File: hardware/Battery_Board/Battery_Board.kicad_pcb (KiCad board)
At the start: 2 copper layers, 83 x 83 mm, 28 parts, among them J1 Source, J3 Battery, P1 USB_C_Plug_USB2.0, Q1 DMG3415U-7, SW3 ON, U4 TP4056

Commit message: feat(Hw):PCB_PwnSat_And_Battery_Updated
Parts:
- moved D4 67.6 mm to (67.0, 146.4), turned to 90 degrees
- moved D3 66.3 mm to (69.9, 146.4), turned to 90 degrees
- moved R31 60.1 mm to (72.1, 145.6), turned to 180 degrees
- moved R33 9.93 mm to (117.6, 108.8), turned to 90 degrees
- moved Q1 7.08 mm to (114.3, 114.7), turned to -90 degrees
- moved D2 2.58 mm to (113.3, 111.0), turned to 0 degrees
- moved C48 2.27 mm to (105.8, 109.7)
- moved C49 1.57 mm to (72.1, 154.9), turned to 180 degrees
- moved R32 1.51 mm to (72.7, 153.7)
- moved R34 1.49 mm to (72.7, 152.8), turned to 180 degrees
- moved R26 0.91 mm to (83.2, 113.0)
- moved F1 0.90 mm to (84.6, 113.0)
- moved R27 0.85 mm to (79.2, 112.2), turned to 0 degrees
- turned R29 to -90 degrees
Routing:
- net +BATT: track 0.00 -> 134.2 mm, vias 0 -> 54
- net /Batt_Connector/USB_DET: track 0.00 -> 90.3 mm
- net VBUS: track 0.00 -> 88.7 mm, vias 0 -> 12
- net /Batt_Connector/Battery: track 0.00 -> 71.6 mm, vias 0 -> 2
- net /Batt_Connector/Enable: track 0.00 -> 65.0 mm
- net VCC: track 0.00 -> 59.2 mm, vias 0 -> 15
- net +3.3V: track 0.00 -> 51.7 mm
- net Net-(D4-K): track 0.00 -> 19.5 mm, vias 0 -> 2
- net Net-(D3-K): track 0.00 -> 16.0 mm, vias 0 -> 2
- net Net-(F1-Pad1): track 0.00 -> 10.3 mm
- net Net-(D2-K): track 0.00 -> 9.72 mm
- net /Batt_Connector/2_DN: track 99.2 -> 105.7 mm
- net Net-(U4-PROG): track 0.00 -> 6.16 mm
- net /Batt_Connector/2_DP: track 99.8 -> 106.0 mm
- net Net-(D3-A): track 0.00 -> 4.28 mm
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- added copper zone on F.Cu, net +3.3V
- added copper zone on B.Cu, net +BATT
- added copper zone on F.Cu, net +BATT
- added copper zone on B.Cu, net GND
- added copper zone on F.Cu, net GND
- added copper zone on B.Cu, net VBUS
- added copper zone on F.Cu, net VBUS
- added copper zone on B.Cu, net VCC
- added copper zone on F.Cu, net VCC

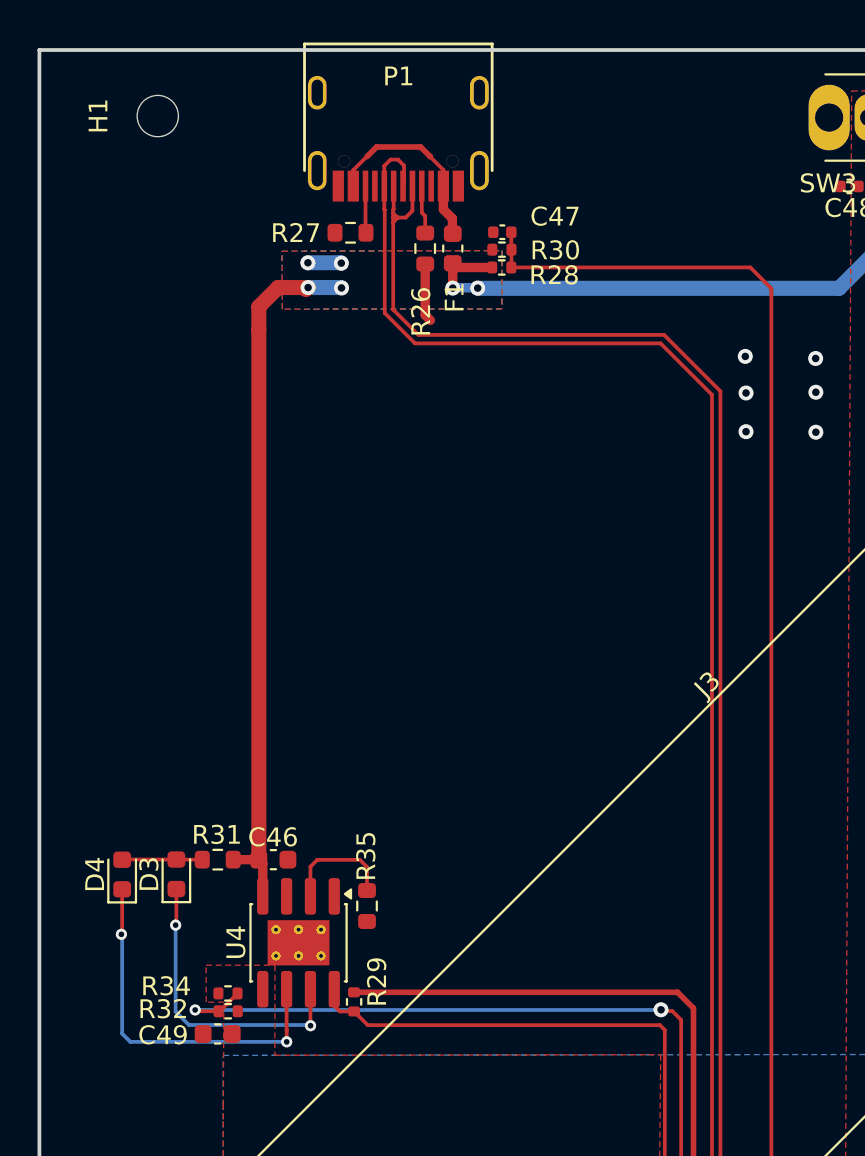
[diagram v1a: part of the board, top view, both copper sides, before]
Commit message: feat(Hw):Boards_Updated
Pending_Sensors_Board
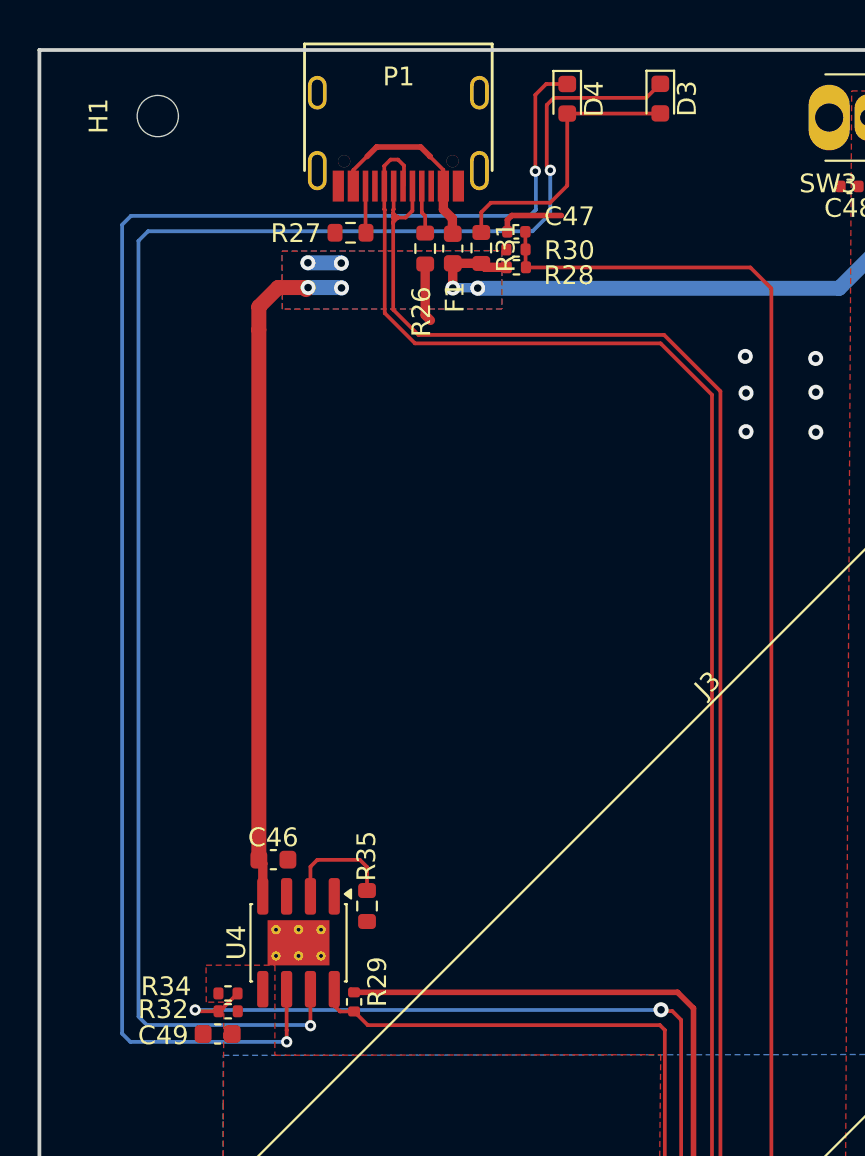
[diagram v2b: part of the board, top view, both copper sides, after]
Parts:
- moved D3 48.7 mm to (95.7, 105.1), turned to -90 degrees
- moved D4 47.7 mm to (90.7, 105.1), turned to -90 degrees
- moved R31 35.5 mm to (86.2, 113.0), turned to 90 degrees
- moved R28 0.78 mm to (88.0, 114.0)
- moved C47 0.75 mm to (88.0, 112.2)
- moved R30 0.75 mm to (88.0, 113.1)
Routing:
- net Net-(D3-K): track 16.0 -> 87.6 mm
- net Net-(D4-K): track 19.5 -> 85.3 mm
- net Net-(D3-A): track 4.28 -> 15.0 mm
- net GND: track 3.12 -> 6.74 mm
- net /Batt_Connector/USB_DET: track 90.3 -> 89.6 mm

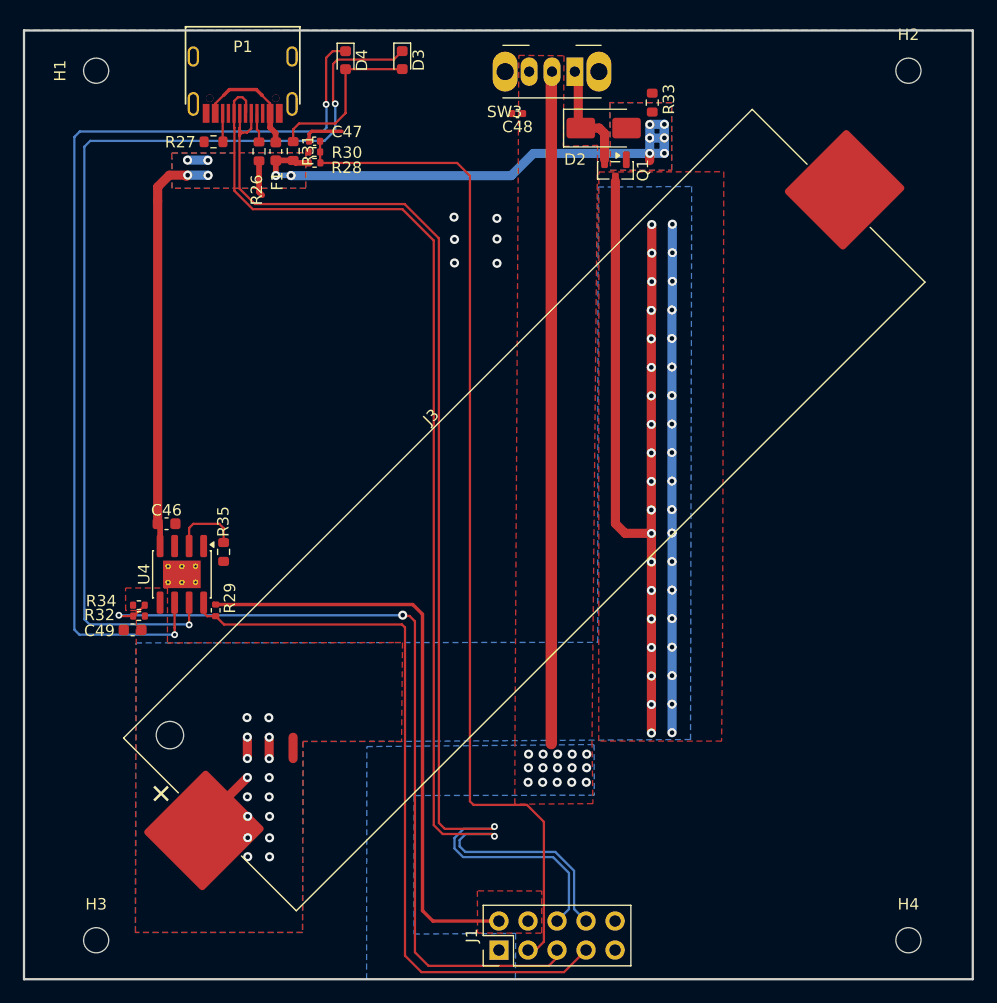
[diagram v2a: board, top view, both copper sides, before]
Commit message: fix(Hw):Tracks_modified
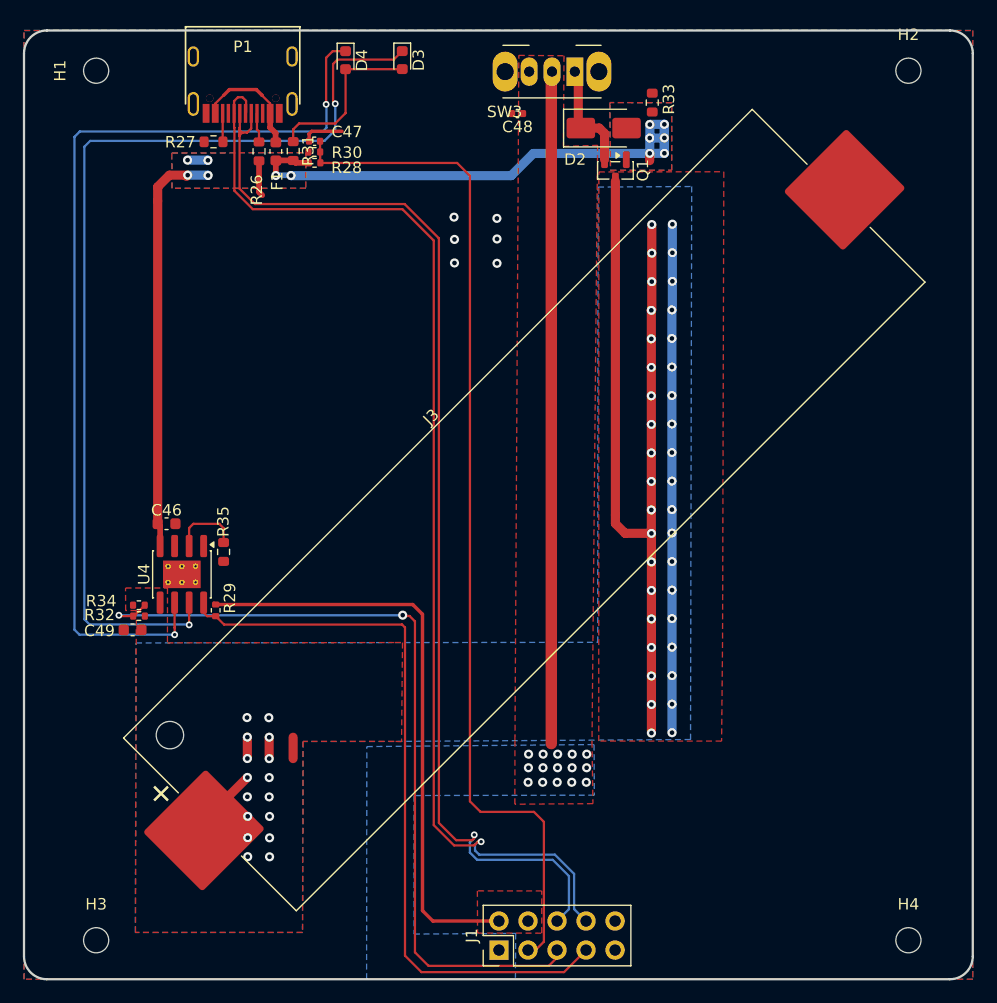
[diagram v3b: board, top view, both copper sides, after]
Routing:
- net /Batt_Connector/2_DN: track 105.7 -> 99.9 mm
- net /Batt_Connector/2_DP: track 106.0 -> 100.8 mm
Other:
- outline, holes or cut-outs redrawn

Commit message: feat(Hw):Labels_Added
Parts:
- added G***: LOGO, Aesthetics:electronic_cats_logo_8x6, F.Cu at (82.4, 126.5)
- added G***: LOGO, Aesthetics:electronic_cats_logo_8x6, B.Cu at (81.5, 120.7)
- added REF**: OSHW-Logo_5.7x6mm_SilkScreen, Symbol:OSHW-Logo_5.7x6mm_SilkScreen, B.Cu at (126.5, 120.0)
- added kibuzzard-698511AF: G***, kibuzzard-698511AF, F.Cu at (117.3, 105.7)
- added kibuzzard-698511C2: G***, kibuzzard-698511C2, F.Cu at (101.1, 105.8)
- added kibuzzard-69851248: G***, kibuzzard-69851248, F.Cu at (82.6, 131.9)
- added kibuzzard-69851248: G***, kibuzzard-69851248, B.Cu at (104.5, 127.2)
- added kibuzzard-6985125C: G***, kibuzzard-6985125C, B.Cu at (104.6, 111.2)
- added kibuzzard-69851454: G***, kibuzzard-69851454, F.Cu at (92.5, 105.3)
- added kibuzzard-69851473: G***, kibuzzard-69851473, F.Cu at (97.5, 105.1)

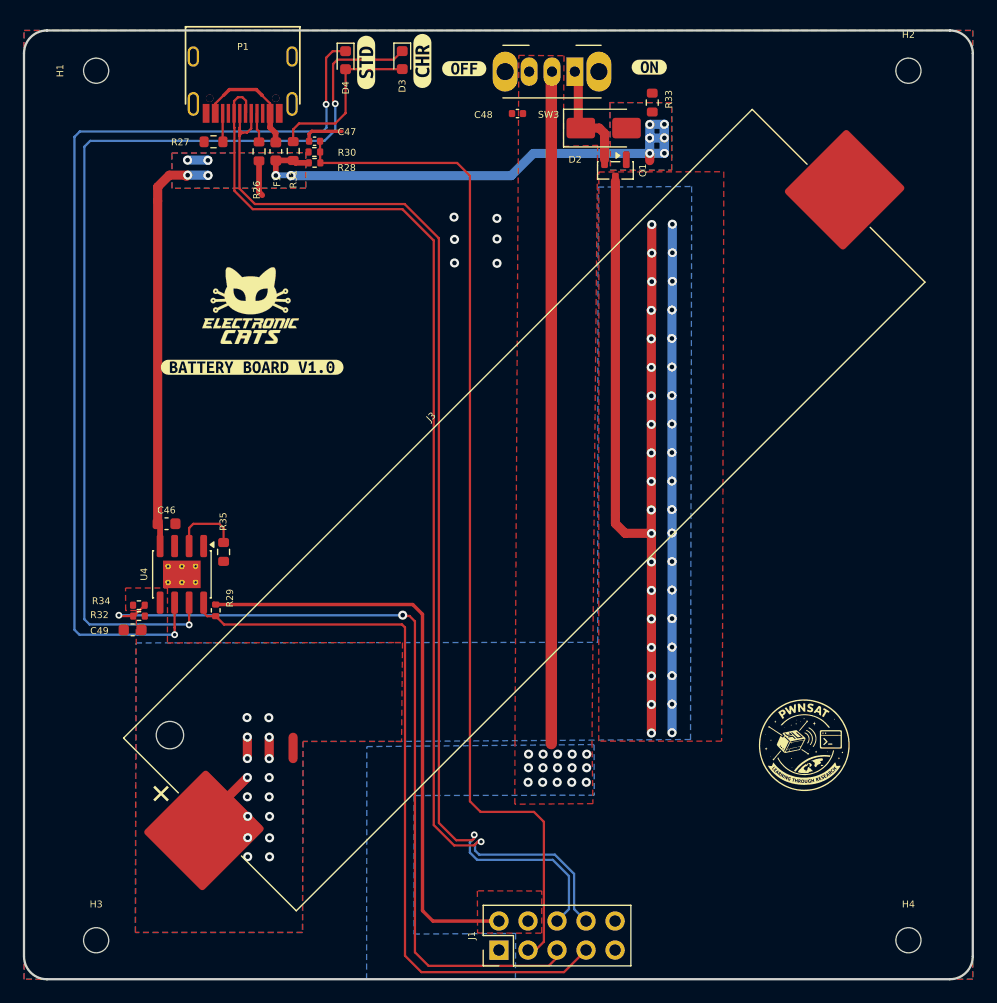
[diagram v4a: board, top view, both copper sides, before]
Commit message: feat(Hw):labels_updated
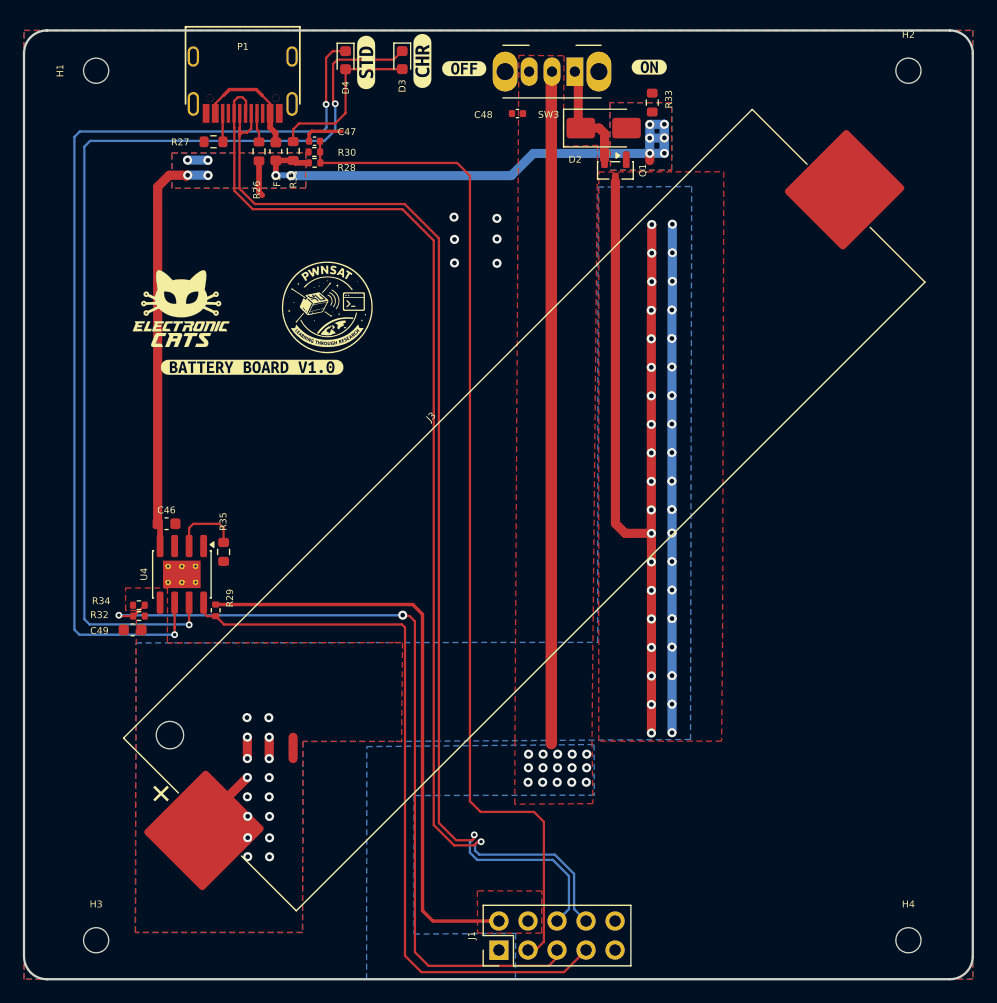
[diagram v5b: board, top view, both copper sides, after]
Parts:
- moved G*** 6.08 mm to (76.3, 126.8)
